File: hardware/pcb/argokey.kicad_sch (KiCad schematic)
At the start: 145 parts

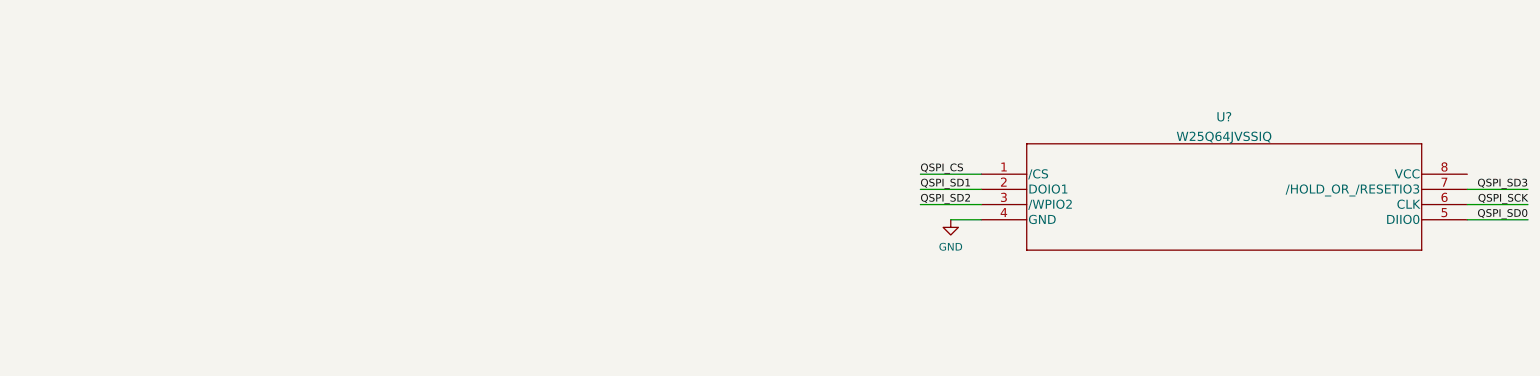
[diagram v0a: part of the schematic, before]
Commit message: Change flash to 16M
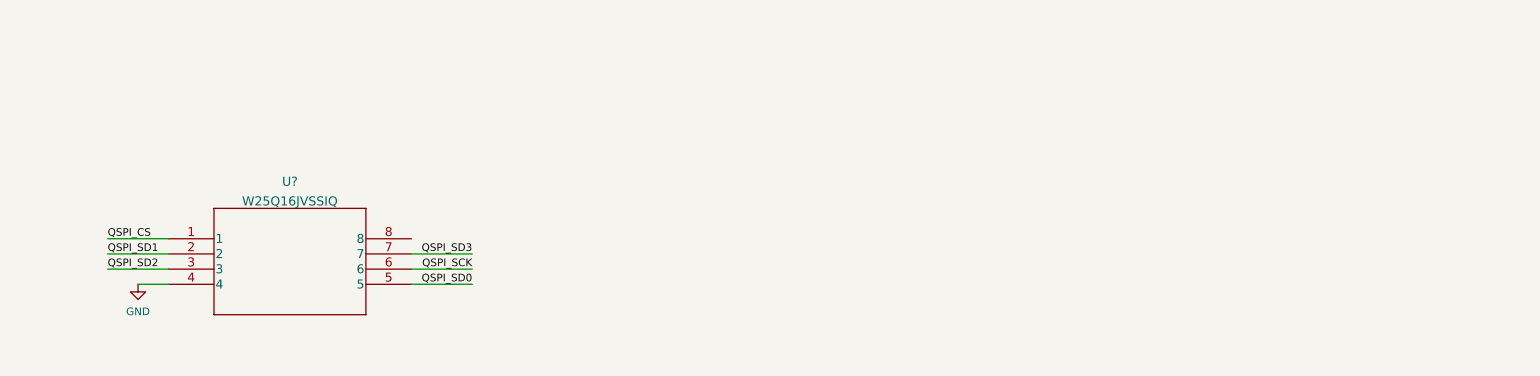
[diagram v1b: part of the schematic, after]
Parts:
- removed U?: W25Q64JVSSIQ, SOIC-8_5P28X5P28_WIN, symbol W25QJVSSIQ:W25Q64JVSSIQ
- added U?: W25Q16JVSSIQ, W25Q16JVSSIQ_WIN, symbol W25Q16JVSSIQ:W25Q16JVSSIQ
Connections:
- net GND: now also U?.4
- net QSPI_CS: now also U?.1
- net QSPI_SCK: now also U?.6
- net QSPI_SD0: now also U?.5
- net QSPI_SD1: now also U?.2
- net QSPI_SD2: now also U?.3
- net QSPI_SD3: now also U?.7
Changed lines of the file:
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@@
     (stroke (width 0) (type default) (color 0 0 0 0))
   )
-  (wire (pts (xy 405.13 235.585) (xy 394.97 235.585))
+  (wire (pts (xy 228.6 246.38) (xy 218.44 246.38))
     (stroke (width 0) (type default) (color 0 0 0 0))
   )
@@
     (stroke (width 0) (type default) (color 0 0 0 0))
   )
-  (wire (pts (xy 405.13 238.125) (xy 394.97 238.125))
+  (wire (pts (xy 228.6 248.92) (xy 218.44 248.92))
     (stroke (width 0) (type default) (color 0 0 0 0))
   )
@@
     (stroke (width 0) (type default) (color 0 0 0 0))
   )
-  (wire (pts (xy 405.13 240.665) (xy 394.97 240.665))
+  (wire (pts (xy 228.6 251.46) (xy 218.44 251.46))
     (stroke (width 0) (type default) (color 0 0 0 0))
   )
@@
     (stroke (width 0) (type default) (color 0 0 0 0))
   )
-  (wire (pts (xy 303.53 238.125) (xy 313.69 238.125))
-    (stroke (width 0) (type default) (color 0 0 0 0))
-  )
   (wire (pts (xy 143.51 25.4) (xy 143.51 36.83))
     (stroke (width 0) (type default) (color 0 0 0 0))
@@
     (stroke (width 0) (type default) (color 0 0 0 0))
   )
+  (wire (pts (xy 167.64 248.92) (xy 177.8 248.92))
+    (stroke (width 0) (type default) (color 0 0 0 0))
+  )
   (wire (pts (xy 160.02 80.01) (xy 163.83 80.01))
     (stroke (width 0) (type default) (color 0 0 0 0))
@@
     (stroke (width 0) (type default) (color 0 0 0 0))
   )
-  (wire (pts (xy 308.61 240.665) (xy 313.69 240.665))
+  (wire (pts (xy 172.72 251.46) (xy 177.8 251.46))
     (stroke (width 0) (type default) (color 0 0 0 0))
   )
@@
     (stroke (width 0) (type default) (color 0 0 0 0))
   )
+  (wire (pts (xy 167.64 246.38) (xy 177.8 246.38))
+    (stroke (width 0) (type default) (color 0 0 0 0))
+  )
   (wire (pts (xy 201.93 115.57) (xy 205.74 115.57))
     (stroke (width 0) (type default) (color 0 0 0 0))
@@
     (stroke (width 0) (type default) (color 0 0 0 0))
   )
-  (wire (pts (xy 303.53 233.045) (xy 313.69 233.045))
+  (wire (pts (xy 167.64 243.84) (xy 177.8 243.84))
     (stroke (width 0) (type default) (color 0 0 0 0))
   )
@@
     (stroke (width 0) (type default) (color 0 0 0 0))
   )
-  (wire (pts (xy 303.53 235.585) (xy 313.69 235.585))
-    (stroke (width 0) (type default) (color 0 0 0 0))
-  )
   (wire (pts (xy 62.23 80.01) (xy 66.04 80.01))
     (stroke (width 0) (type default) (color 0 0 0 0))
@@
     (effects (font (size 1.27 1.27)) (justify right bottom))
   )
-  (label "QSPI_SD3" (at 405.13 235.585 180)
+  (label "QSPI_SD3" (at 228.6 246.38 180)
     (effects (font (size 1.27 1.27)) (justify right bottom))
   )
@@
     (effects (font (size 1.27 1.27)) (justify right bottom))
   )
-  (label "QSPI_CS" (at 303.53 233.045 0)
+  (label "QSPI_CS" (at 167.64 243.84 0)
     (effects (font (size 1.27 1.27)) (justify left bottom))
   )
-  (label "QSPI_SD1" (at 303.53 235.585 0)
+  (label "QSPI_SD1" (at 167.64 246.38 0)
     (effects (font (size 1.27 1.27)) (justify left bottom))
   )
@@
     (effects (font (size 1.27 1.27)) (justify right bottom))
   )
-  (label "QSPI_SD2" (at 303.53 238.125 0)
+  (label "QSPI_SD2" (at 167.64 248.92 0)
     (effects (font (size 1.27 1.27)) (justify left bottom))
   )
-  (label "QSPI_SD0" (at 405.13 240.665 180)
+  (label "QSPI_SD0" (at 228.6 251.46 180)
     (effects (font (size 1.27 1.27)) (justify right bottom))
   )
-  (label "QSPI_SCK" (at 405.13 238.125 180)
+  (label "QSPI_SCK" (at 228.6 248.92 180)
     (effects (font (size 1.27 1.27)) (justify right bottom))
   )
@@
     (pin "2")
   )
-  (symbol (lib_id "W25QJVSSIQ:W25Q64JVSSIQ") (at 313.69 233.045 0) (unit 1)
-    (in_bom yes) (on_board yes) (fields_autoplaced)
-    (property "Reference" "U?" (id 0) (at 354.33 223.4976 0)
-      (effects (font (size 1.524 1.524)))
-    )
-    (property "Value" "W25Q64JVSSIQ" (id 1) (at 354.33 226.7766 0)
-      (effects (font (size 1.524 1.524)))
-    )
-    (property "Footprint" "SOIC-8_5P28X5P28_WIN" (id 2) (at 354.33 226.949 0)
-      (effects (font (size 1.524 1.524)) hide)
-    )
-    (property "Datasheet" "" (id 3) (at 313.69 233.045 0)
-      (effects (font (size 1.524 1.524)))
-    )
-    (pin "1")
-    (pin "2")
-    (pin "3")
-    (pin "4")
-    (pin "5")
-    (pin "6")
-    (pin "7")
-    (pin "8")
-  )
   (symbol (lib_id "Device:C_Small") (at 52.07 147.955 90) (unit 1)
     (in_bom yes) (on_board yes)
@@
     (pin "2")
   )
+  (symbol (lib_id "W25Q16JVSSIQ:W25Q16JVSSIQ") (at 177.8 243.84 0) (unit 1)
+    (in_bom yes) (on_board yes) (fields_autoplaced)
+    (property "Reference" "U?" (id 0) (at 198.12 234.2926 0)
+      (effects (font (size 1.524 1.524)))
+    )
+    (property "Value" "W25Q16JVSSIQ" (id 1) (at 198.12 237.5716 0)
+      (effects (font (size 1.524 1.524)))
+    )
+    (property "Footprint" "W25Q16JVSSIQ_WIN" (id 2) (at 198.12 237.744 0)
+      (effects (font (size 1.524 1.524)) hide)
+    )
+    (property "Datasheet" "" (id 3) (at 177.8 243.84 0)
+      (effects (font (size 1.524 1.524)))
+    )
+    (pin "1")
+    (pin "2")
+    (pin "3")
+    (pin "4")
+    (pin "5")
+    (pin "6")
+    (pin "7")
+    (pin "8")
+  )
   (symbol (lib_id "KeySwitch:Switch") (at 67.31 55.88 0) (unit 1)
     (in_bom yes) (on_board yes)
@@
     (pin "2")
   )
-  (symbol (lib_id "power:GND") (at 308.61 240.665 0) (unit 1)
+  (symbol (lib_id "power:GND") (at 172.72 251.46 0) (unit 1)
     (in_bom yes) (on_board yes) (fields_autoplaced)
-    (property "Reference" "#PWR?" (id 0) (at 308.61 247.015 0)
+    (property "Reference" "#PWR?" (id 0) (at 172.72 257.81 0)
       (effects (font (size 1.27 1.27)) hide)
     )
-    (property "Value" "GND" (id 1) (at 308.61 245.2275 0))
-    (property "Footprint" "" (id 2) (at 308.61 240.665 0)
+    (property "Value" "GND" (id 1) (at 172.72 256.0225 0))
+    (property "Footprint" "" (id 2) (at 172.72 251.46 0)
       (effects (font (size 1.27 1.27)) hide)
     )
-    (property "Datasheet" "" (id 3) (at 308.61 240.665 0)
+    (property "Datasheet" "" (id 3) (at 172.72 251.46 0)
       (effects (font (size 1.27 1.27)) hide)
     )
@@
       (reference "SW?") (unit 1) (value "RotaryEncoder_Switch") (footprint "")
     )
-    (path "/70046ad5-b979-40fd-9768-260cf4098b67"
-      (reference "U?") (unit 1) (value "W25Q64JVSSIQ") (footprint "SOIC-8_5P28X5P28_WIN")
-    )
     (path "/98069f1a-fd7f-4370-8100-b340393cbef7"
       (reference "U?") (unit 1) (value "RP2040") (footprint "IC57_RP2040")
     )
+    (path "/d7e7b640-da59-4ecd-ad2d-9e7ff15404b8"
+      (reference "U?") (unit 1) (value "W25Q16JVSSIQ") (footprint "W25Q16JVSSIQ_WIN")
+    )
   )

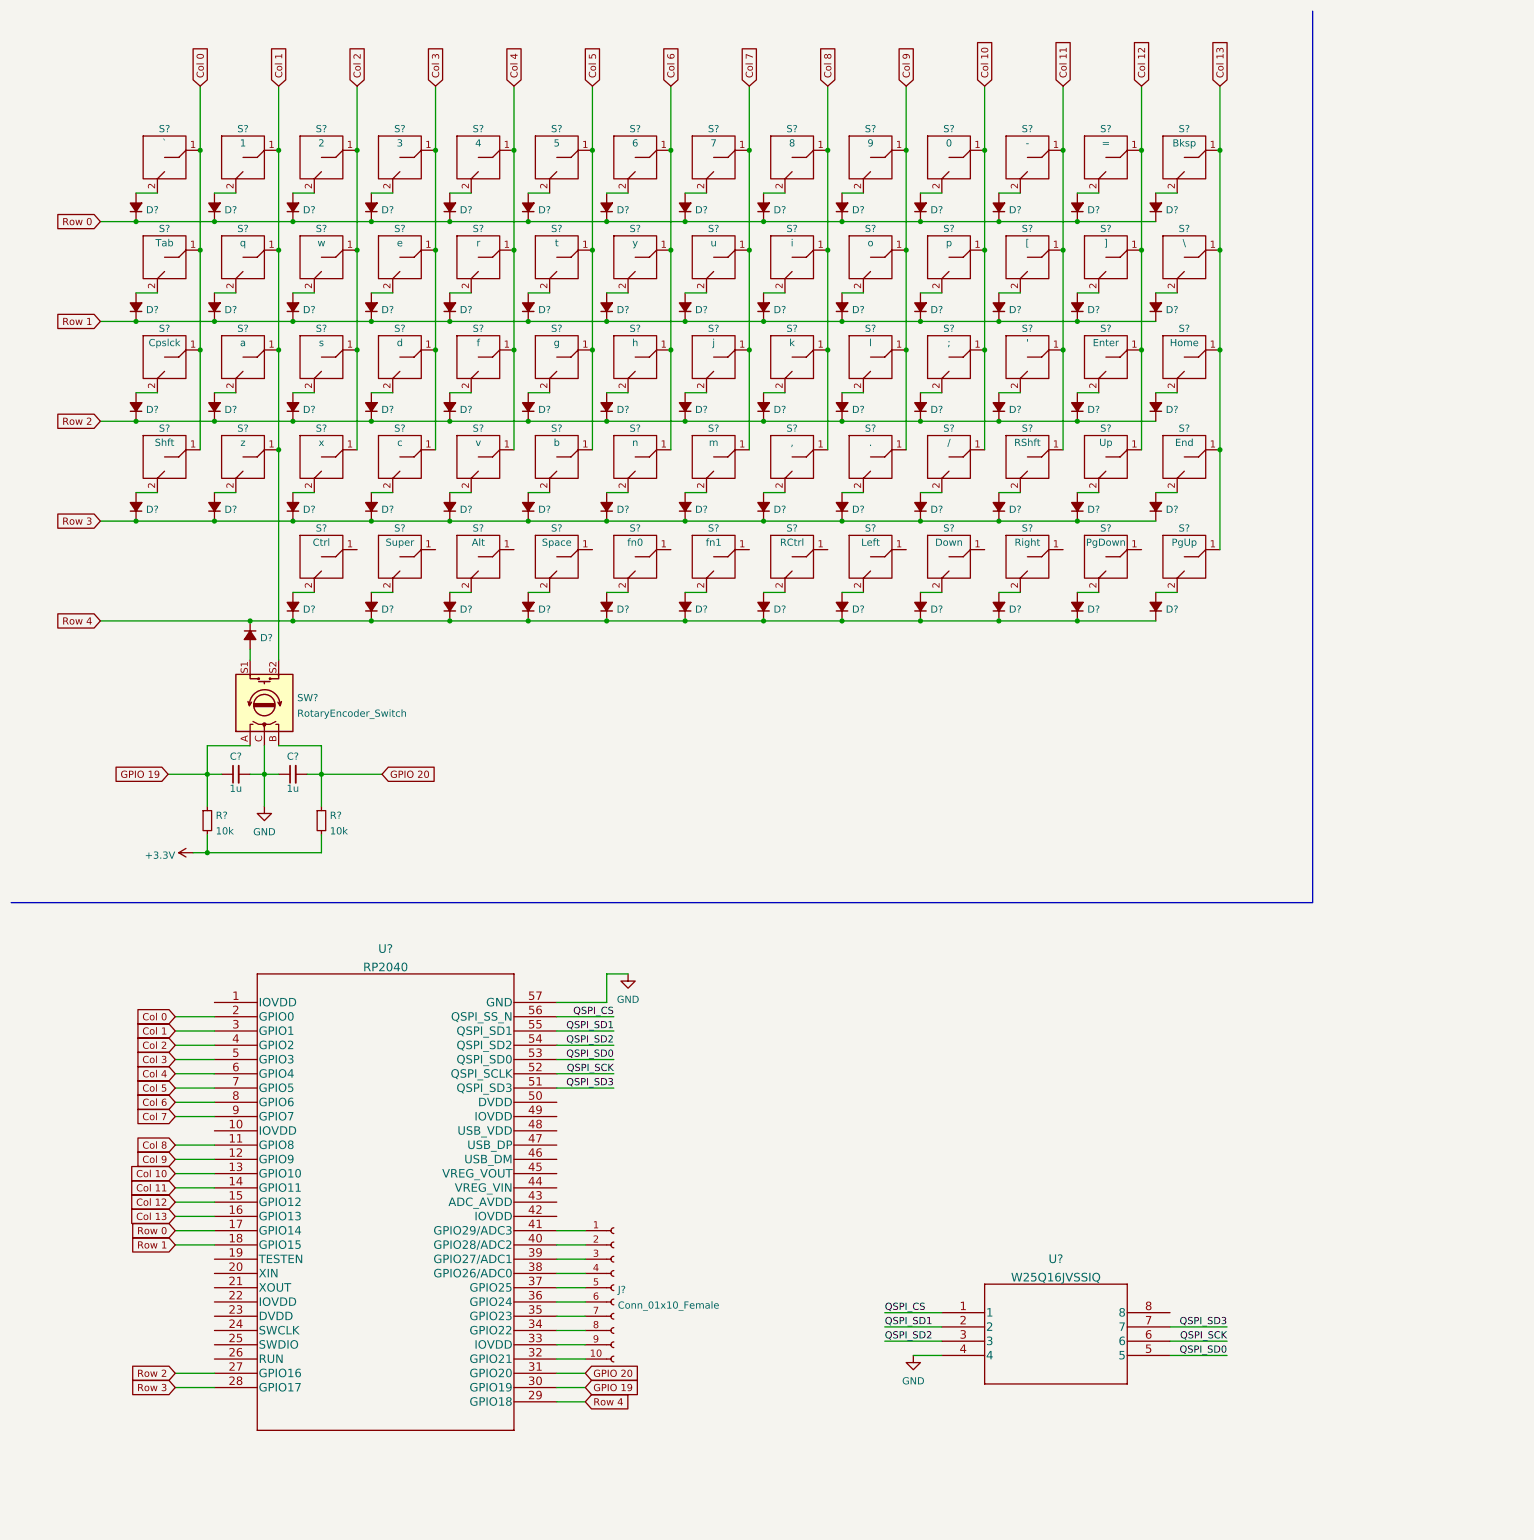
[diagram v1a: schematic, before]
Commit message: Schematic: RP2040 Power
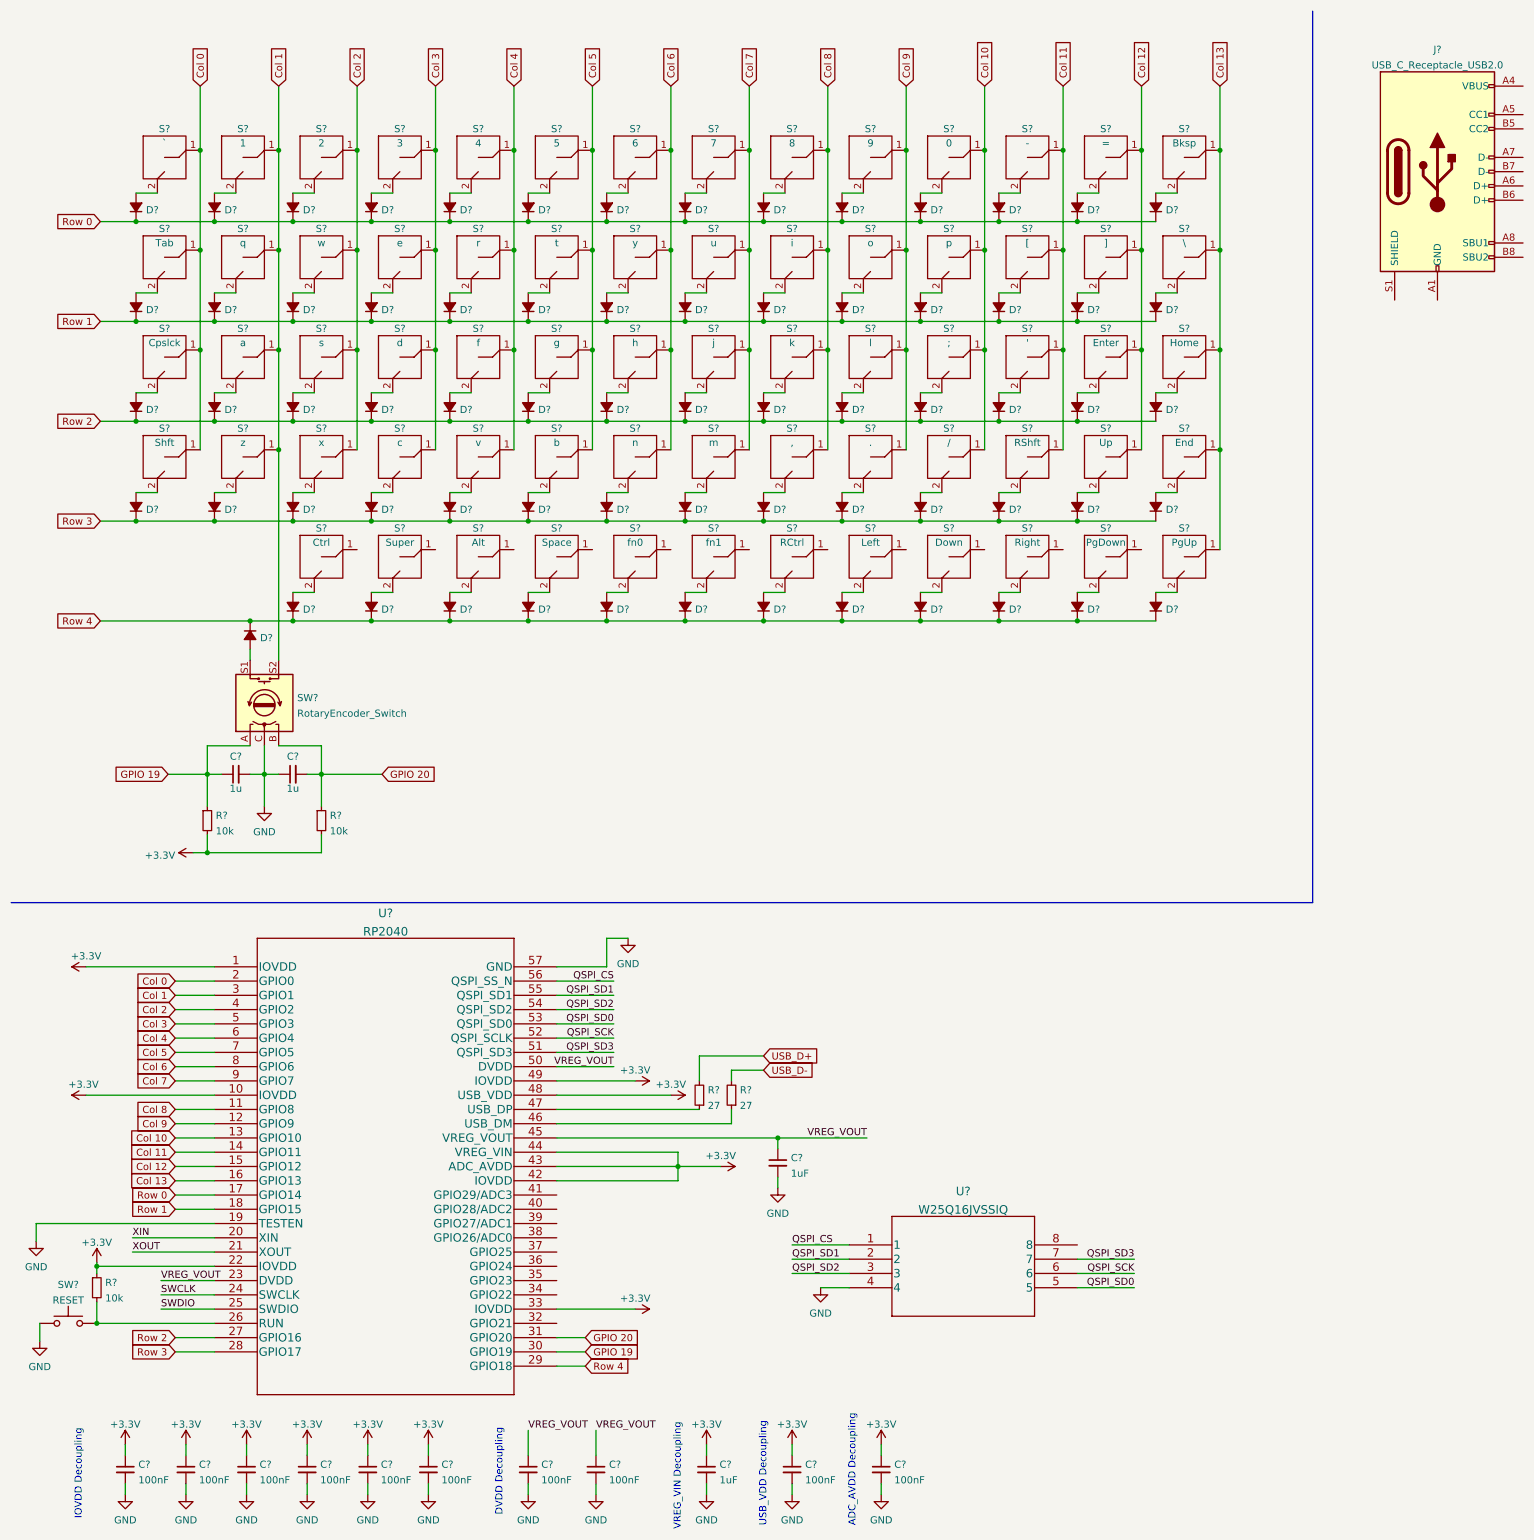
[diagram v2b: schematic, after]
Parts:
- removed J?: Conn_01x10_Female, symbol Connector:Conn_01x10_Female
- added C? (x10): 100nF, symbol Device:C_Small
- added C? (x2): 1uF, symbol Device:C_Small
- added J?: USB_C_Receptacle_USB2.0, symbol Connector:USB_C_Receptacle_USB2.0
- added R?: 10k, symbol Device:R_Small
- added R? (x2): 27, symbol Device:R_Small
- added SW?: RESET, symbol Switch:SW_Push
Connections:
- net +3V3: now also U?.1 (IOVDD), U?.10 (IOVDD), U?.22 (IOVDD), U?.33 (IOVDD), U?.42 (IOVDD), U?.43 (ADC_AVDD), U?.44 (VREG_VIN), U?.48 (USB_VDD), U?.49 (IOVDD), C?.1, C?.1, C?.1, C?.1, C?.1, C?.1, C?.1, C?.1, C?.1, R?.1
- net GND: now also U?.19 (TESTEN), C?.2, C?.2, C?.2, C?.2, C?.2, C?.2, C?.2, C?.2, C?.2, C?.2, C?.2, C?.2, SW?.1
- net XIN: now reaches U?.20 (XIN)
- net XOUT: now reaches U?.21 (XOUT)
- net VREG_VOUT: now reaches U?.23 (DVDD)
- net VREG_VOUT: now also U?.45 (VREG_VOUT), U?.50 (DVDD), C?.1, C?.1, C?.1
- net SWCLK: now reaches U?.24 (SWCLK)
- net SWDIO: now reaches U?.25 (SWDIO)
- net at U?.26 (RUN): now also R?.2, SW?.2
- net at U?.46 (USB_DM): now also R?.1
- net at U?.47 (USB_DP): now also R?.1
- new net: J?.A1 (GND), J?.A12 (GND), J?.B1 (GND), J?.B12 (GND)
- new net: J?.A4 (VBUS), J?.A9 (VBUS), J?.B4 (VBUS), J?.B9 (VBUS)
- new net USB_D+: R?.2
- new net USB_D-: R?.2
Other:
- note added: "ADC_AVDD Decoupling"
- note added: "DVDD Decoupling"
- note added: "IOVDD Decoupling"
- note added: "USB_VDD Decoupling"
- note added: "VREG_VIN Decoupling"
- moved on the sheet: U?

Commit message: Rev 1 Schematic
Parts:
- added C13, C14: 27p, symbol Device:C_Small
- added C15, C18: 10u, symbol Device:C_Small
- added C3: 100n, symbol Device:C_Small
- added J1: USB_BOOT, symbol Connector:Conn_01x02_Male
- added R3, R8: 1k, symbol Device:R_Small
- added R4: 10k DNF, symbol Device:R_Small
- added R6, R7: 5.1k, symbol Device:R_Small
- added U3: NCP1117-3.3_SOT223, Package_TO_SOT_SMD:SOT-223-3_TabPin2, symbol Regulator_Linear:NCP1117-3.3_SOT223
- added Y1: ABLS-12.000MHZ-B4-T, symbol Device:Crystal
- C10, C11, C12, C16, C17, C5, C6, C7, C8, C9: renamed from C?; value 100nF -> 100n
- C19, C4: renamed from C?; value 1uF -> 1u
- gave numbers to parts that had none: 149
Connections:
- net +3V3: now also U1.8, C18.1, C3.1, R4.1, U3.2 (VO)
- net GND: now also J2.A1 (GND), J2.A12 (GND), J2.B1 (GND), J2.B12 (GND), C13.1, C14.1, C15.2, C18.2, C3.2, J1.2 (Pin_2), R6.1, R7.1, U3.1 (GND)
- net GPIO 19: no longer U2.30 (GPIO19)
- net GPIO 20: no longer U2.31 (GPIO20)
- net QSPI_CS: now also R3.1, R4.2
- net USB_D+: now also J2.A6 (D+), J2.B6 (D+)
- net USB_D-: now also J2.A7 (D-), J2.B7 (D-)
- net XIN: now also C13.2, Y1.2
- net XOUT: now also R8.2
- net OLED_SCL: now reaches U2.32 (GPIO21)
- net VBUS: now reaches J2.A4 (VBUS), J2.A9 (VBUS), J2.B4 (VBUS), J2.B9 (VBUS)
- net VBUS: now also C15.1, U3.3 (VI)
- net at J2.A5 (CC1): now also R7.2
- net at J2.B5 (CC2): now also R6.2
- net Earth: now reaches J2.S1 (SHIELD)
- new net: C14.2, R8.1, Y1.1
- new net: J1.1 (Pin_1), R3.2
- new net OLED_SDA: U2.31 (GPIO20)
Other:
- note added: "Crystal"
- note added: "Flash Memory"
- note added: "Keyboard"
- note added: "RP2040"
- note added: "USB"
- company: (none) -> Argonaut Labs
- title: (none) -> RP2040-Based Custom Keyboard
- moved on the sheet: C1, C10, C11, C12, C16, C17, C19, C2, C4, C5, C6, C7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
